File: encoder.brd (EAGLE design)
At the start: 26.2 x 31.4 mm, 5 parts

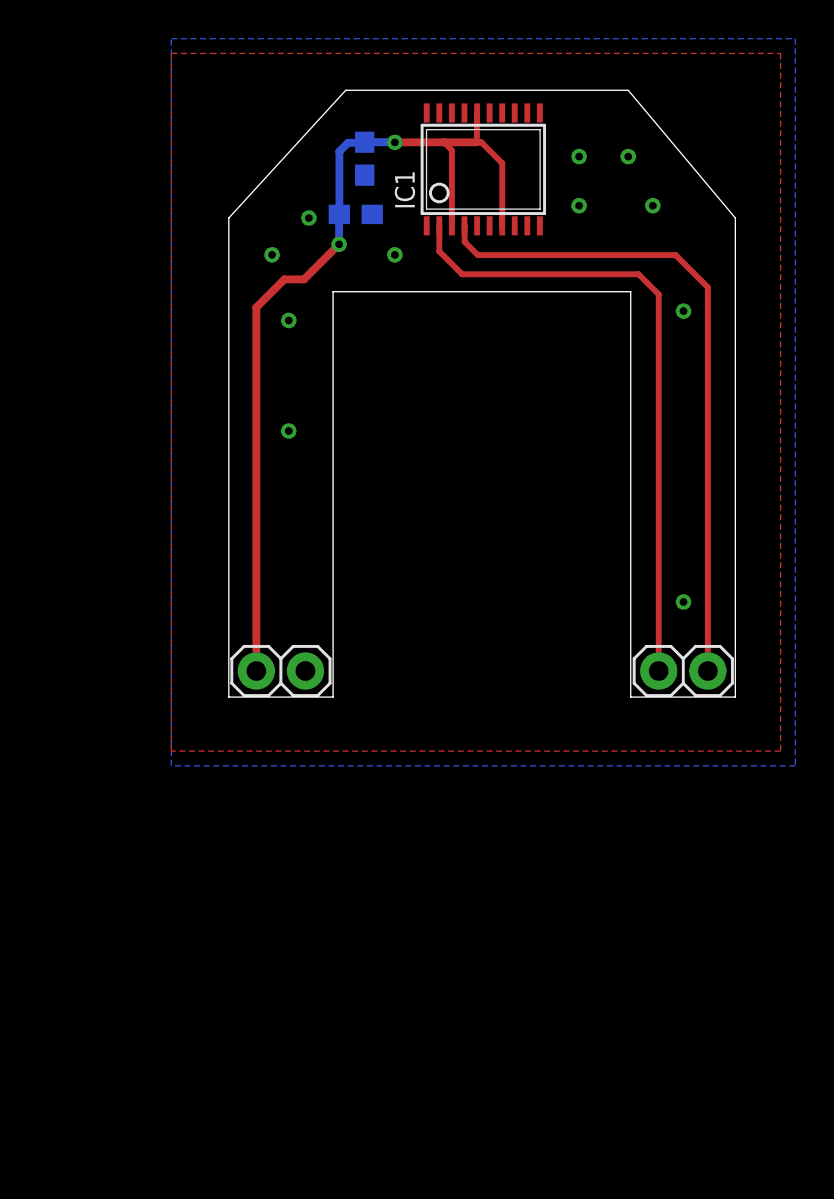
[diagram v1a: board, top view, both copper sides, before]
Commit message: poprawa bledow, dodanie rezystorow na wyjsciach stm-glownie w modolach, poprawa elementu 9axis z biblioteki
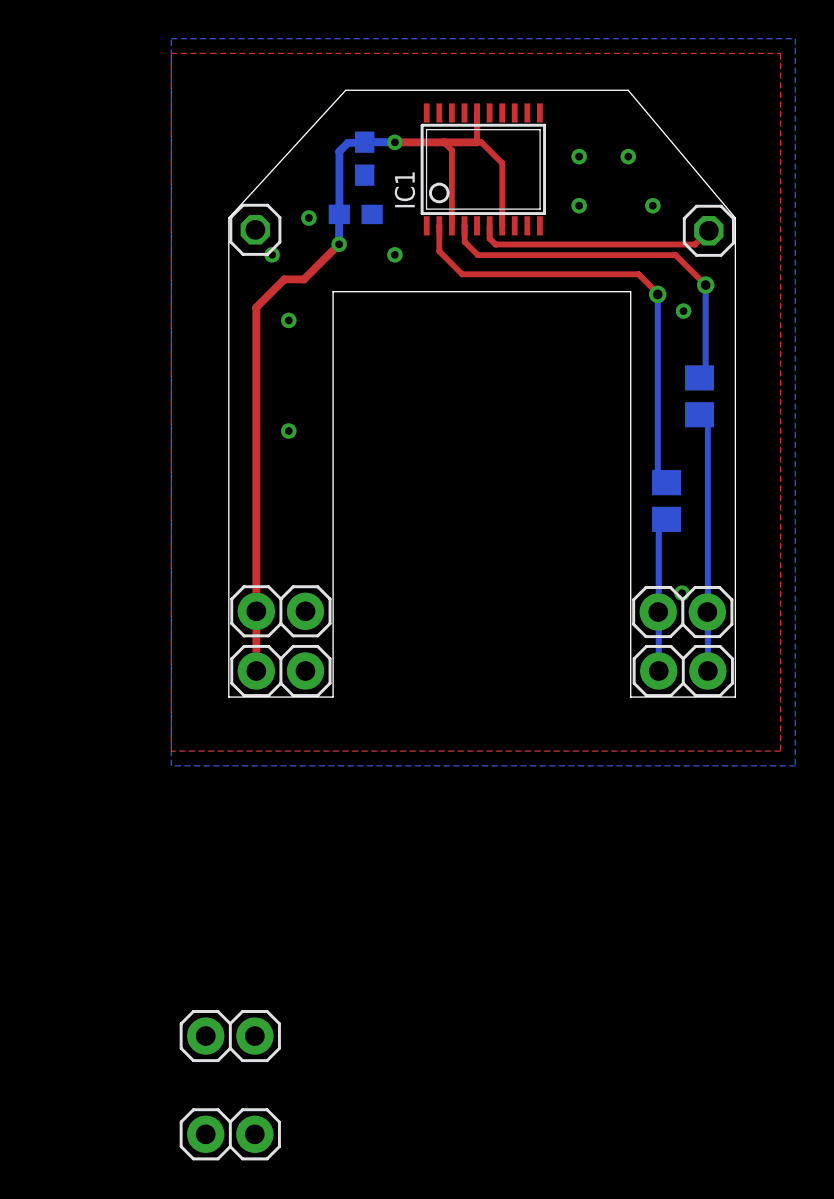
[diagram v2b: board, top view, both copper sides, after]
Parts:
- added JP3, JP8: (no value), pinhead:1X01
- added JP4, JP5, JP6, JP7: PINHD_1X2_ROUND, _microMouse:PINHD_1X2_ROUND
- added R1, R2: (no value), rcl:R0805
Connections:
- new net AO: IC1.AO, JP3.1
- new net N$1: JP2.1, R1.1
- new net N$2: JP2.2, R2.2
- net CHA: now also R1.2; no longer JP2.1
- net CHB: now also R2.1; no longer JP2.2
- net GND: now also JP4.2, JP8.1
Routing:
- net CHB: track 34.2 -> 19.4 mm, vias 0 -> 1
- net N$2: track 0.00 -> 13.4 mm
- net AO: track 0.00 -> 12.4 mm
- net CHA: track 33.1 -> 23.6 mm, vias 0 -> 1
- net N$1: track 0.00 -> 8.01 mm
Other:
- board text added: "+5V"
- board text added: "A"
- board text added: "Analog Output"
- board text added: "B"
- board text added: "GND"
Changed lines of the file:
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@@
 <setting verticaltext="up"/>
 </settings>
-<grid distance="10" unitdist="mil" unit="mil" style="lines" multiple="1" display="yes" altdistance="1" altunitdist="mil" altunit="mil"/>
+<grid distance="3" unitdist="mil" unit="mil" style="lines" multiple="1" display="yes" altdistance="1" altunitdist="mil" altunit="mil"/>
 <layers>
 <layer number="1" name="Top" color="4" fill="1" visible="yes" active="yes"/>
@@
 <layer number="25" name="tNames" color="7" fill="1" visible="yes" active="yes"/>
 <layer number="26" name="bNames" color="7" fill="1" visible="yes" active="yes"/>
-<layer number="27" name="tValues" color="7" fill="1" visible="yes" active="yes"/>
-<layer number="28" name="bValues" color="7" fill="1" visible="yes" active="yes"/>
+<layer number="27" name="tValues" color="7" fill="1" visible="no" active="yes"/>
+<layer number="28" name="bValues" color="7" fill="1" visible="no" active="yes"/>
 <layer number="29" name="tStop" color="7" fill="3" visible="no" active="yes"/>
 <layer number="30" name="bStop" color="7" fill="6" visible="no" active="yes"/>
@@
 <wire x1="15.875" y1="31.369" x2="9.8298" y2="24.765" width="0" layer="20"/>
 <wire x1="9.8298" y1="24.765" x2="9.8298" y2="0" width="0" layer="20"/>
+<text x="33.2232" y="22.9362" size="1.27" layer="26" rot="MR0">Analog Output</text>
+<text x="14.2494" y="20.8788" size="1.27" layer="26" rot="MR0">GND</text>
+<text x="11.811" y="9.525" size="1.27" layer="22" rot="MR270">+5V</text>
+<text x="14.3256" y="9.9822" size="1.27" layer="22" rot="MR270">GND</text>
+<text x="32.6898" y="6.3246" size="1.27" layer="22" rot="MR0">A</text>
+<text x="35.1282" y="6.1722" size="1.27" layer="22" rot="MR0">B</text>
 </plain>
 <attributes>
@@
 </autorouter>
 <elements>
-<element name="C1" library="rcl" package="C0603" value="10u" x="16.854" y="27.8326" rot="MR270"/>
-<element name="C2" library="rcl" package="C0603" value="100n" x="16.3942" y="24.9502" rot="MR180"/>
-<element name="IC1" library="_microMouse" package="TSSOP20" value="" x="22.987" y="27.2786"/>
+<element name="C1" library="rcl" package="C0603" value="10u" x="16.854" y="27.8326" smashed="yes" rot="MR270">
+<attribute name="NAME" x="16.0666" y="28.9248" size="1.27" layer="26" rot="MR270"/>
+<attribute name="VALUE" x="18.759" y="28.4676" size="1.27" layer="28" rot="MR270"/>
+</element>
+<element name="C2" library="rcl" package="C0603" value="100n" x="16.3942" y="24.9502" smashed="yes" rot="MR180">
+<attribute name="NAME" x="15.9878" y="24.239" size="1.27" layer="26" rot="MR180"/>
+<attribute name="VALUE" x="15.7592" y="26.8552" size="1.27" layer="28" rot="MR180"/>
+</element>
+<element name="IC1" library="_microMouse" package="TSSOP20" value="" x="22.987" y="27.2786" smashed="yes">
+<attribute name="NAME" x="19.4414" y="25.1958" size="1.016" layer="25" ratio="10" rot="R90"/>
+<attribute name="VALUE" x="27.5232" y="25.1958" size="1.016" layer="27" ratio="10" rot="R90"/>
+</element>
 <element name="JP1" library="_microMouse" package="PINHD_1X2_ROUND" value="PINHD_1X2_ROUND" x="13.7922" y="1.3462"/>
 <element name="JP2" library="_microMouse" package="PINHD_1X2_ROUND" value="PINHD_1X2_ROUND" x="34.5948" y="1.3462"/>
+<element name="R1" library="rcl" package="R0805" value="" x="32.4612" y="10.1346" rot="MR90"/>
+<element name="R2" library="rcl" package="R0805" value="" x="34.163" y="15.5448" rot="MR270"/>
+<element name="JP3" library="pinhead" package="1X01" value="" x="34.6456" y="24.1046" smashed="yes">
+<attribute name="VALUE" x="33.3756" y="20.9296" size="1.27" layer="27"/>
+</element>
+<element name="JP4" library="_microMouse" package="PINHD_1X2_ROUND" value="PINHD_1X2_ROUND" x="13.7922" y="4.4323"/>
+<element name="JP5" library="_microMouse" package="PINHD_1X2_ROUND" value="PINHD_1X2_ROUND" x="34.5694" y="4.3942"/>
+<element name="JP6" library="_microMouse" package="PINHD_1X2_ROUND" value="PINHD_1X2_ROUND" x="11.176" y="-17.526"/>
+<element name="JP7" library="_microMouse" package="PINHD_1X2_ROUND" value="PINHD_1X2_ROUND" x="11.176" y="-22.606"/>
+<element name="JP8" library="pinhead" package="1X01" value="" x="11.2014" y="24.1554" smashed="yes">
+<attribute name="VALUE" x="9.9314" y="20.9804" size="1.27" layer="27"/>
+</element>
 </elements>
 <signals>
@@
 <via x="27.94" y="27.94" extent="1-16" drill="0.4"/>
 <via x="33.3375" y="19.9517" extent="1-16" drill="0.4"/>
-<via x="33.3375" y="4.9149" extent="1-16" drill="0.4"/>
+<via x="33.2613" y="5.3721" extent="1-16" drill="0.4"/>
 <via x="12.9286" y="13.7541" extent="1-16" drill="0.4"/>
 <via x="12.9286" y="19.4691" extent="1-16" drill="0.4"/>
@@
 <vertex x="6.858" y="-3.556"/>
 </polygon>
+<contactref element="JP8" pad="1"/>
+<contactref element="JP4" pad="2"/>
 </signal>
 <signal name="CHA">
 <contactref element="IC1" pad="A"/>
-<contactref element="JP2" pad="1"/>
 <wire x1="20.712" y1="24.3608" x2="20.7137" y2="24.3591" width="0.3048" layer="1"/>
 <wire x1="20.7137" y1="24.3591" x2="20.7137" y2="23.0378" width="0.3048" layer="1"/>
 <wire x1="20.7137" y1="23.0378" x2="21.8948" y2="21.8567" width="0.3048" layer="1"/>
 <wire x1="21.8948" y1="21.8567" x2="31.0134" y2="21.8567" width="0.3048" layer="1"/>
-<wire x1="31.0134" y1="21.8567" x2="32.0548" y2="20.8153" width="0.3048" layer="1"/>
-<wire x1="32.0548" y1="20.8153" x2="32.0548" y2="1.3462" width="0.3048" layer="1"/>
+<contactref element="R1" pad="2"/>
+<wire x1="32.004" y1="20.8153" x2="32.0548" y2="20.8153" width="0.254" layer="16"/>
+<wire x1="32.004" y1="20.7645" x2="32.0548" y2="20.8153" width="0.3048" layer="16"/>
+<wire x1="31.0134" y1="21.8567" x2="32.004" y2="20.8661" width="0.3048" layer="1"/>
+<wire x1="32.004" y1="20.8661" x2="32.004" y2="20.8153" width="0.3048" layer="1"/>
+<via x="32.004" y="20.8153" extent="1-16" drill="0.5" shape="octagon"/>
+<wire x1="32.004" y1="20.8153" x2="32.004" y2="20.7645" width="0.3048" layer="16"/>
+<wire x1="32.004" y1="20.7645" x2="32.004" y2="11.5418" width="0.3048" layer="16"/>
+<wire x1="32.004" y1="11.5418" x2="32.4612" y2="11.0846" width="0.3048" layer="16"/>
 </signal>
 <signal name="CHB">
 <contactref element="IC1" pad="B"/>
-<contactref element="JP2" pad="2"/>
 <wire x1="22.012" y1="24.3608" x2="22.0218" y2="24.351" width="0.3048" layer="1"/>
 <wire x1="22.0218" y1="24.351" x2="22.0218" y2="23.5331" width="0.3048" layer="1"/>
 <wire x1="22.0218" y1="23.5331" x2="22.7076" y2="22.8473" width="0.3048" layer="1"/>
 <wire x1="22.7076" y1="22.8473" x2="32.9311" y2="22.8473" width="0.3048" layer="1"/>
-<wire x1="32.9311" y1="22.8473" x2="34.5948" y2="21.1836" width="0.3048" layer="1"/>
-<wire x1="34.5948" y1="21.1836" x2="34.5948" y2="1.3462" width="0.3048" layer="1"/>
+<wire x1="32.9311" y1="22.8473" x2="34.4805" y2="21.2979" width="0.3048" layer="1"/>
+<contactref element="R2" pad="1"/>
+<wire x1="34.4805" y1="21.2979" x2="34.5948" y2="21.1836" width="0.3048" layer="1"/>
+<wire x1="34.544" y1="21.2344" x2="34.4805" y2="21.2979" width="0.3048" layer="16"/>
+<via x="34.4805" y="21.2979" extent="1-16" drill="0.5" shape="octagon"/>
+<wire x1="34.163" y1="16.4948" x2="34.4805" y2="16.8123" width="0.3048" layer="16"/>
+<wire x1="34.4805" y1="16.8123" x2="34.4805" y2="21.2979" width="0.3048" layer="16"/>
 </signal>
 <signal name="VCC">
@@
 <wire x1="11.2522" y1="20.1422" x2="11.2522" y2="1.3462" width="0.4064" layer="1"/>
 </signal>
+<signal name="N$1">
+<contactref element="JP2" pad="1"/>
+<contactref element="R1" pad="1"/>
+<wire x1="32.4612" y1="9.1846" x2="32.0548" y2="8.7782" width="0.3048" layer="16"/>
+<wire x1="32.0548" y1="8.7782" x2="32.0548" y2="1.3462" width="0.3048" layer="16"/>
+</signal>
+<signal name="N$2">
+<contactref element="JP2" pad="2"/>
+<contactref element="R2" pad="2"/>
+<wire x1="34.5948" y1="1.3462" x2="34.5948" y2="14.163" width="0.3048" layer="16"/>
+<wire x1="34.5948" y1="14.163" x2="34.163" y2="14.5948" width="0.3048" layer="16"/>
+</signal>
+<signal name="AO">
+<contactref element="IC1" pad="AO"/>
+<contactref element="JP3" pad="1"/>
+<wire x1="23.312" y1="24.3608" x2="23.312" y2="23.7034" width="0.3048" layer="1"/>
+<wire x1="23.312" y1="23.7034" x2="23.622" y2="23.3934" width="0.3048" layer="1"/>
+<wire x1="23.622" y1="23.3934" x2="33.9344" y2="23.3934" width="0.3048" layer="1"/>
+<wire x1="33.9344" y1="23.3934" x2="34.6456" y2="24.1046" width="0.3048" layer="1"/>
+</signal>
 </signals>

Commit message: gerbery
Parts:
- moved JP6 31.6 mm to (34.6, 3.66)
- moved JP7 26.3 mm to (13.8, 3.58)
- moved JP4 4.65 mm to (13.7, 9.08)
- moved JP5 4.65 mm to (34.5, 9.04)
- moved R1 2.90 mm to (32.4, 13.0)
- moved R2 1.91 mm to (34.2, 17.4)
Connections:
- net GND: now also JP7.2
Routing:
- net N$1: track 8.01 -> 11.0 mm
- net CHA: track 23.6 -> 20.7 mm
- net N$2: track 13.4 -> 15.3 mm
- net CHB: track 19.4 -> 17.7 mm
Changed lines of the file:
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@@
 <text x="33.2232" y="22.9362" size="1.27" layer="26" rot="MR0">Analog Output</text>
 <text x="14.2494" y="20.8788" size="1.27" layer="26" rot="MR0">GND</text>
-<text x="11.811" y="9.525" size="1.27" layer="22" rot="MR270">+5V</text>
-<text x="14.3256" y="9.9822" size="1.27" layer="22" rot="MR270">GND</text>
+<text x="11.7348" y="14.1732" size="1.27" layer="22" rot="MR270">+5V</text>
+<text x="14.3256" y="14.478" size="1.27" layer="22" rot="MR270">GND</text>
 <text x="32.6898" y="6.3246" size="1.27" layer="22" rot="MR0">A</text>
 <text x="35.1282" y="6.1722" size="1.27" layer="22" rot="MR0">B</text>
@@
 <element name="JP1" library="_microMouse" package="PINHD_1X2_ROUND" value="PINHD_1X2_ROUND" x="13.7922" y="1.3462"/>
 <element name="JP2" library="_microMouse" package="PINHD_1X2_ROUND" value="PINHD_1X2_ROUND" x="34.5948" y="1.3462"/>
-<element name="R1" library="rcl" package="R0805" value="" x="32.4612" y="10.1346" rot="MR90"/>
-<element name="R2" library="rcl" package="R0805" value="" x="34.163" y="15.5448" rot="MR270"/>
+<element name="R1" library="rcl" package="R0805" value="" x="32.385" y="13.0302" rot="MR90"/>
+<element name="R2" library="rcl" package="R0805" value="" x="34.2392" y="17.4498" rot="MR270"/>
 <element name="JP3" library="pinhead" package="1X01" value="" x="34.6456" y="24.1046" smashed="yes">
 <attribute name="VALUE" x="33.3756" y="20.9296" size="1.27" layer="27"/>
 </element>
-<element name="JP4" library="_microMouse" package="PINHD_1X2_ROUND" value="PINHD_1X2_ROUND" x="13.7922" y="4.4323"/>
-<element name="JP5" library="_microMouse" package="PINHD_1X2_ROUND" value="PINHD_1X2_ROUND" x="34.5694" y="4.3942"/>
-<element name="JP6" library="_microMouse" package="PINHD_1X2_ROUND" value="PINHD_1X2_ROUND" x="11.176" y="-17.526"/>
-<element name="JP7" library="_microMouse" package="PINHD_1X2_ROUND" value="PINHD_1X2_ROUND" x="11.176" y="-22.606"/>
+<element name="JP4" library="_microMouse" package="PINHD_1X2_ROUND" value="PINHD_1X2_ROUND" x="13.716" y="9.0805"/>
+<element name="JP5" library="_microMouse" package="PINHD_1X2_ROUND" value="PINHD_1X2_ROUND" x="34.4932" y="9.0424"/>
 <element name="JP8" library="pinhead" package="1X01" value="" x="11.2014" y="24.1554" smashed="yes">
 <attribute name="VALUE" x="9.9314" y="20.9804" size="1.27" layer="27"/>
 </element>
+<element name="JP6" library="_microMouse" package="PINHD_1X2_ROUND" value="PINHD_1X2_ROUND" x="34.5948" y="3.6576"/>
+<element name="JP7" library="_microMouse" package="PINHD_1X2_ROUND" value="PINHD_1X2_ROUND" x="13.7922" y="3.5814"/>
 </elements>
 <signals>
@@
 <via x="27.94" y="27.94" extent="1-16" drill="0.4"/>
 <via x="33.3375" y="19.9517" extent="1-16" drill="0.4"/>
-<via x="33.2613" y="5.3721" extent="1-16" drill="0.4"/>
-<via x="12.9286" y="13.7541" extent="1-16" drill="0.4"/>
+<via x="12.4714" y="15.7353" extent="1-16" drill="0.4"/>
 <via x="12.9286" y="19.4691" extent="1-16" drill="0.4"/>
 <polygon width="0.3048" layer="1" isolate="0.254">
@@
 <contactref element="JP8" pad="1"/>
 <contactref element="JP4" pad="2"/>
+<contactref element="JP7" pad="2"/>
 </signal>
 <signal name="CHA">
@@
 <via x="32.004" y="20.8153" extent="1-16" drill="0.5" shape="octagon"/>
 <wire x1="32.004" y1="20.8153" x2="32.004" y2="20.7645" width="0.3048" layer="16"/>
-<wire x1="32.004" y1="20.7645" x2="32.004" y2="11.5418" width="0.3048" layer="16"/>
-<wire x1="32.004" y1="11.5418" x2="32.4612" y2="11.0846" width="0.3048" layer="16"/>
+<wire x1="32.004" y1="20.7645" x2="32.004" y2="14.4374" width="0.3048" layer="16"/>
+<wire x1="32.004" y1="14.4374" x2="32.385" y2="13.9802" width="0.3048" layer="16"/>
 </signal>
 <signal name="CHB">
@@
 <wire x1="34.544" y1="21.2344" x2="34.4805" y2="21.2979" width="0.3048" layer="16"/>
 <via x="34.4805" y="21.2979" extent="1-16" drill="0.5" shape="octagon"/>
-<wire x1="34.163" y1="16.4948" x2="34.4805" y2="16.8123" width="0.3048" layer="16"/>
-<wire x1="34.4805" y1="16.8123" x2="34.4805" y2="21.2979" width="0.3048" layer="16"/>
+<wire x1="34.2392" y1="18.3998" x2="34.4805" y2="18.3363" width="0.3048" layer="16"/>
+<wire x1="34.4805" y1="18.3363" x2="34.4805" y2="21.2979" width="0.3048" layer="16"/>
 </signal>
 <signal name="VCC">
@@
 <contactref element="JP2" pad="1"/>
 <contactref element="R1" pad="1"/>
-<wire x1="32.4612" y1="9.1846" x2="32.0548" y2="8.7782" width="0.3048" layer="16"/>
-<wire x1="32.0548" y1="8.7782" x2="32.0548" y2="1.3462" width="0.3048" layer="16"/>
+<wire x1="32.385" y1="12.0802" x2="32.0548" y2="11.9786" width="0.3048" layer="16"/>
+<wire x1="32.0548" y1="11.9786" x2="32.0548" y2="1.3462" width="0.3048" layer="16"/>
 </signal>
 <signal name="N$2">
 <contactref element="JP2" pad="2"/>
 <contactref element="R2" pad="2"/>
-<wire x1="34.5948" y1="1.3462" x2="34.5948" y2="14.163" width="0.3048" layer="16"/>
-<wire x1="34.5948" y1="14.163" x2="34.163" y2="14.5948" width="0.3048" layer="16"/>
+<wire x1="34.5948" y1="1.3462" x2="34.5948" y2="16.068" width="0.3048" layer="16"/>
+<wire x1="34.5948" y1="16.068" x2="34.2392" y2="16.4998" width="0.3048" layer="16"/>
 </signal>
 <signal name="AO">

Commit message: zamiana warstw
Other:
- board text added: "C1"
- board text added: "C2"
- board text added: "IC1"
- board text added: "R1"
- board text added: "R2"
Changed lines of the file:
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@@
 <layer number="123" name="tTestmark" color="7" fill="1" visible="yes" active="yes"/>
 <layer number="124" name="bTestmark" color="7" fill="1" visible="yes" active="yes"/>
-<layer number="125" name="_tNames" color="7" fill="1" visible="yes" active="yes"/>
-<layer number="126" name="_bNames" color="7" fill="1" visible="yes" active="yes"/>
-<layer number="127" name="_tValues" color="7" fill="1" visible="yes" active="yes"/>
+<layer number="125" name="_tNames" color="14" fill="1" visible="yes" active="yes"/>
+<layer number="126" name="_bNames" color="5" fill="1" visible="yes" active="yes"/>
+<layer number="127" name="_tValues" color="14" fill="1" visible="yes" active="yes"/>
 <layer number="128" name="_bValues" color="7" fill="1" visible="yes" active="yes"/>
 <layer number="129" name="Mask" color="7" fill="1" visible="yes" active="yes"/>
@@
 <text x="32.6898" y="6.3246" size="1.27" layer="22" rot="MR0">A</text>
 <text x="35.1282" y="6.1722" size="1.27" layer="22" rot="MR0">B</text>
+<text x="16.06659375" y="28.924809375" size="1.27" layer="126" rot="MR270">C1</text>
+<text x="15.9878" y="24.238990625" size="1.27" layer="126" rot="MR180">C2</text>
+<text x="19.4413875" y="25.195809375" size="1.016" layer="125" ratio="10" rot="R90">IC1</text>
+<text x="33.655" y="12.3952" size="1.27" layer="126" rot="MR90">R1</text>
+<text x="32.9692" y="18.0848" size="1.27" layer="126" rot="MR270">R2</text>
 </plain>
 <attributes>
